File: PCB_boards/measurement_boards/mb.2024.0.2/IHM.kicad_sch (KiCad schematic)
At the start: 8 parts

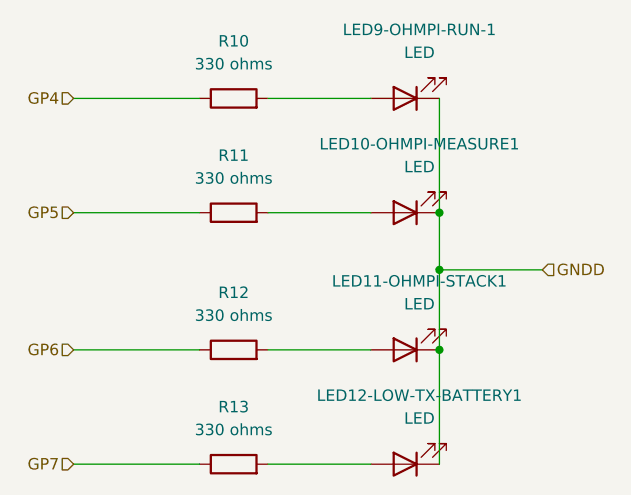
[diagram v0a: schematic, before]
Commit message: correction DPS, add dischage resistor, remove 63 warning on the schemtic, remove 7 errors in schematics change resistor designation, update pcb
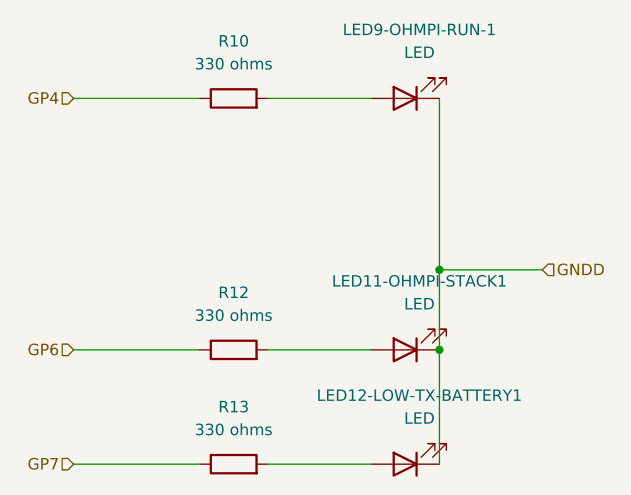
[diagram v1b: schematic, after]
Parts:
- removed LED10-OHMPI-MEASURE1: LED, LED_THT:LED_D4.0mm, symbol Device:LED
- removed R11: 330 ohms, Resistor_THT:R_Axial_DIN0207_L6.3mm_D2.5mm_P7.62mm_Horizontal, symbol Device:R
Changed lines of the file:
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@@
 (kicad_sch (version 20230121) (generator eeschema)
   (paper "A4")
-  (junction (at 152.4 77.47) (diameter 0) (color 0 0 0 0)
-  )
   (junction (at 152.4 92.71) (diameter 0) (color 0 0 0 0)
   )
@@
     (stroke (width 0) (type default))
   )
-  (wire (pts (xy 152.4 77.47) (xy 152.4 83.82))
+  (wire (pts (xy 152.4 64.77) (xy 152.4 83.82))
     (stroke (width 0) (type default))
   )
@@
     (stroke (width 0) (type default))
   )
-  (wire (pts (xy 152.4 64.77) (xy 152.4 77.47))
-    (stroke (width 0) (type default))
-  )
   (wire (pts (xy 111.76 64.77) (xy 125.73 64.77))
     (stroke (width 0) (type default))
   )
-  (wire (pts (xy 111.76 77.47) (xy 125.73 77.47))
-    (stroke (width 0) (type default))
-  )
   (wire (pts (xy 152.4 83.82) (xy 152.4 92.71))
     (stroke (width 0) (type default))
   )
   (wire (pts (xy 152.4 83.82) (xy 163.83 83.82))
-    (stroke (width 0) (type default))
-  )
-  (wire (pts (xy 133.35 77.47) (xy 144.78 77.47))
     (stroke (width 0) (type default))
   )
@@
     (effects (font (size 1.27 1.27)) (justify right))
   )
-  (hierarchical_label "GP5" (shape input) (at 111.76 77.47 180) (fields_autoplaced)
-    (effects (font (size 1.27 1.27)) (justify right))
-  )
   (symbol (lib_id "Device:R") (at 129.54 64.77 90) (unit 1)
     (in_bom yes) (on_board yes) (dnp no) (fields_autoplaced)
@@
         )
       )
-    )
-  )
-  (symbol (lib_id "Device:R") (at 129.54 77.47 90) (unit 1)
-    (in_bom yes) (on_board yes) (dnp no) (fields_autoplaced)
-    (property "Reference" "R11" (at 129.54 71.12 90)
-      (effects (font (size 1.27 1.27)))
-    )
-    (property "Value" "330 ohms" (at 129.54 73.66 90)
-      (effects (font (size 1.27 1.27)))
-    )
-    (property "Footprint" "Resistor_THT:R_Axial_DIN0207_L6.3mm_D2.5mm_P7.62mm_Horizontal" (at 129.54 79.248 90)
-      (effects (font (size 1.27 1.27)) hide)
-    )
-    (property "Datasheet" "~" (at 129.54 77.47 0)
-      (effects (font (size 1.27 1.27)) hide)
-    )
-    (property "Description" "330 ohms resistor" (at 129.54 77.47 90)
-      (effects (font (size 1.27 1.27)) hide)
-    )
-    (pin "1")
-    (pin "2")
-    (instances
-      (project "mb.2024.0.2"
-        (path "/62d2b953-c7cc-4d07-805d-38225011d95a/b5055e4e-7413-40b3-89ed-dfdcecf2a97c"
-          (reference "R11") (unit 1)
-        )
-      )
-    )
-  )
-  (symbol (lib_id "Device:LED") (at 148.59 77.47 180) (unit 1)
-    (in_bom yes) (on_board yes) (dnp no) (fields_autoplaced)
-    (property "Reference" "LED10-OHMPI-MEASURE1" (at 150.1775 69.85 0)
-      (effects (font (size 1.27 1.27)))
-    )
-    (property "Value" "LED" (at 150.1775 72.39 0)
-      (effects (font (size 1.27 1.27)))
-    )
-    (property "Footprint" "LED_THT:LED_D4.0mm" (at 148.59 77.47 0)
-      (effects (font (size 1.27 1.27)) hide)
-    )
-    (property "Datasheet" "~" (at 148.59 77.47 0)
-      (effects (font (size 1.27 1.27)) hide)
-    )
-    (property "Description" "LED" (at 148.59 77.47 0)
-      (effects (font (size 1.27 1.27)) hide)
-    )
-    (pin "1")
-    (pin "2")
-    (instances
-      (project "mb.2024.0.2"
-        (path "/62d2b953-c7cc-4d07-805d-38225011d95a/b5055e4e-7413-40b3-89ed-dfdcecf2a97c"
-          (reference "LED10-OHMPI-MEASURE1") (unit 1)
-        )
-      )

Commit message: update measurement board
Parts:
- added LED10-OHMPI-MEASURE1: LED, LED_THT:LED_D4.0mm, symbol Device:LED
- added R11: 330 ohms, Resistor_THT:R_Axial_DIN0207_L6.3mm_D2.5mm_P7.62mm_Horizontal, symbol Device:R
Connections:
- net GNDD: now also LED10-OHMPI-MEASURE1.1 (K)
- new net: LED10-OHMPI-MEASURE1.2 (A), R11.2
- new net GP5: R11.1
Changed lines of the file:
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@@
 (kicad_sch (version 20230121) (generator eeschema)
   (paper "A4")
+  (junction (at 152.4 77.47) (diameter 0) (color 0 0 0 0)
+  )
   (junction (at 152.4 92.71) (diameter 0) (color 0 0 0 0)
   )
@@
     (stroke (width 0) (type default))
   )
-  (wire (pts (xy 152.4 64.77) (xy 152.4 83.82))
+  (wire (pts (xy 152.4 77.47) (xy 152.4 83.82))
     (stroke (width 0) (type default))
   )
@@
     (stroke (width 0) (type default))
   )
+  (wire (pts (xy 152.4 64.77) (xy 152.4 77.47))
+    (stroke (width 0) (type default))
+  )
   (wire (pts (xy 111.76 64.77) (xy 125.73 64.77))
     (stroke (width 0) (type default))
   )
+  (wire (pts (xy 111.76 77.47) (xy 125.73 77.47))
+    (stroke (width 0) (type default))
+  )
   (wire (pts (xy 152.4 83.82) (xy 152.4 92.71))
     (stroke (width 0) (type default))
   )
   (wire (pts (xy 152.4 83.82) (xy 163.83 83.82))
+    (stroke (width 0) (type default))
+  )
+  (wire (pts (xy 133.35 77.47) (xy 144.78 77.47))
     (stroke (width 0) (type default))
   )
@@
     (effects (font (size 1.27 1.27)) (justify right))
   )
+  (hierarchical_label "GP5" (shape input) (at 111.76 77.47 180) (fields_autoplaced)
+    (effects (font (size 1.27 1.27)) (justify right))
+  )
   (symbol (lib_id "Device:R") (at 129.54 64.77 90) (unit 1)
     (in_bom yes) (on_board yes) (dnp no) (fields_autoplaced)
@@
         )
       )
+    )
+  )
+  (symbol (lib_id "Device:R") (at 129.54 77.47 90) (unit 1)
+    (in_bom yes) (on_board yes) (dnp no) (fields_autoplaced)
+    (property "Reference" "R11" (at 129.54 71.12 90)
+      (effects (font (size 1.27 1.27)))
+    )
+    (property "Value" "330 ohms" (at 129.54 73.66 90)
+      (effects (font (size 1.27 1.27)))
+    )
+    (property "Footprint" "Resistor_THT:R_Axial_DIN0207_L6.3mm_D2.5mm_P7.62mm_Horizontal" (at 129.54 79.248 90)
+      (effects (font (size 1.27 1.27)) hide)
+    )
+    (property "Datasheet" "~" (at 129.54 77.47 0)
+      (effects (font (size 1.27 1.27)) hide)
+    )
+    (property "Description" "330 ohms resistor" (at 129.54 77.47 90)
+      (effects (font (size 1.27 1.27)) hide)
+    )
+    (pin "1")
+    (pin "2")
+    (instances
+      (project "mb.2024.0.2"
+        (path "/62d2b953-c7cc-4d07-805d-38225011d95a/b5055e4e-7413-40b3-89ed-dfdcecf2a97c"
+          (reference "R11") (unit 1)
+        )
+      )
+    )
+  )
+  (symbol (lib_id "Device:LED") (at 148.59 77.47 180) (unit 1)
+    (in_bom yes) (on_board yes) (dnp no) (fields_autoplaced)
+    (property "Reference" "LED10-OHMPI-MEASURE1" (at 150.1775 69.85 0)
+      (effects (font (size 1.27 1.27)))
+    )
+    (property "Value" "LED" (at 150.1775 72.39 0)
+      (effects (font (size 1.27 1.27)))
+    )
+    (property "Footprint" "LED_THT:LED_D4.0mm" (at 148.59 77.47 0)
+      (effects (font (size 1.27 1.27)) hide)
+    )
+    (property "Datasheet" "~" (at 148.59 77.47 0)
+      (effects (font (size 1.27 1.27)) hide)
+    )
+    (property "Description" "LED" (at 148.59 77.47 0)
+      (effects (font (size 1.27 1.27)) hide)
+    )
+    (pin "1")
+    (pin "2")
+    (instances
+      (project "mb.2024.0.2"
+        (path "/62d2b953-c7cc-4d07-805d-38225011d95a/b5055e4e-7413-40b3-89ed-dfdcecf2a97c"
+          (reference "LED10-OHMPI-MEASURE1") (unit 1)
+        )
+      )
